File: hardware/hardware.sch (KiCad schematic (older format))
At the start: 54 parts, among them J1 BATT, J2 RFID-RC522, J3 104031-0811, J4 PROG, J5 Conn_01x05_Male, J6 PCM5102A_1, J7 PCM5102A_2, J8 Speakers, SW1 Vol down, SW2 Vol up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

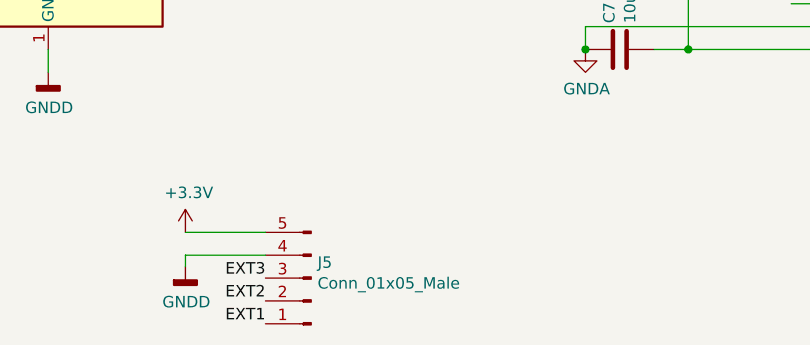
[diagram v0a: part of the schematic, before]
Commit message: fix name of EXT header
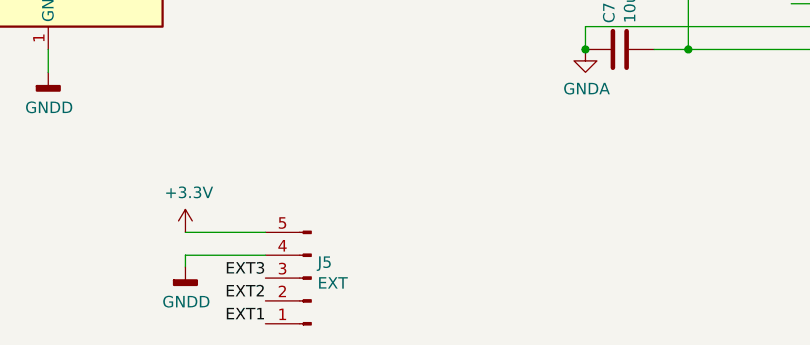
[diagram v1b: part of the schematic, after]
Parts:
- J5: value Conn_01x05_Male -> EXT
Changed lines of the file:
@@
 P 6050 7150
 F 0 "J5" H 6022 7082 50  0000 R CNN
-F 1 "Conn_01x05_Male" H 6022 7173 50  0000 R CNN
+F 1 "EXT" H 6022 7173 50  0000 R CNN
 F 2 "" H 6050 7150 50  0001 C CNN
 F 3 "~" H 6050 7150 50  0001 C CNN

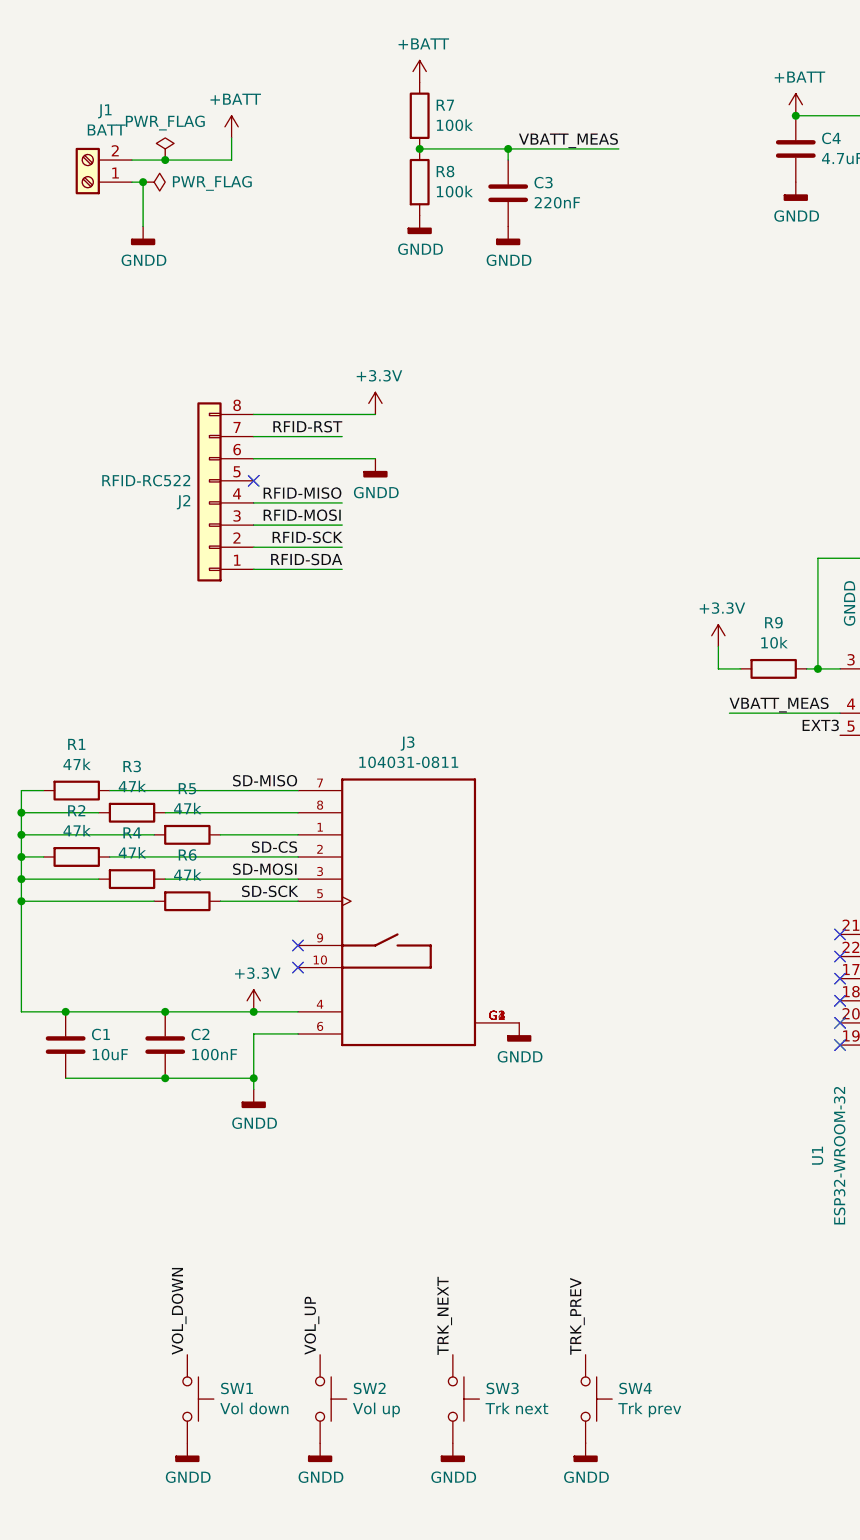
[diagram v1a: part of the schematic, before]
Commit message: layout corrections
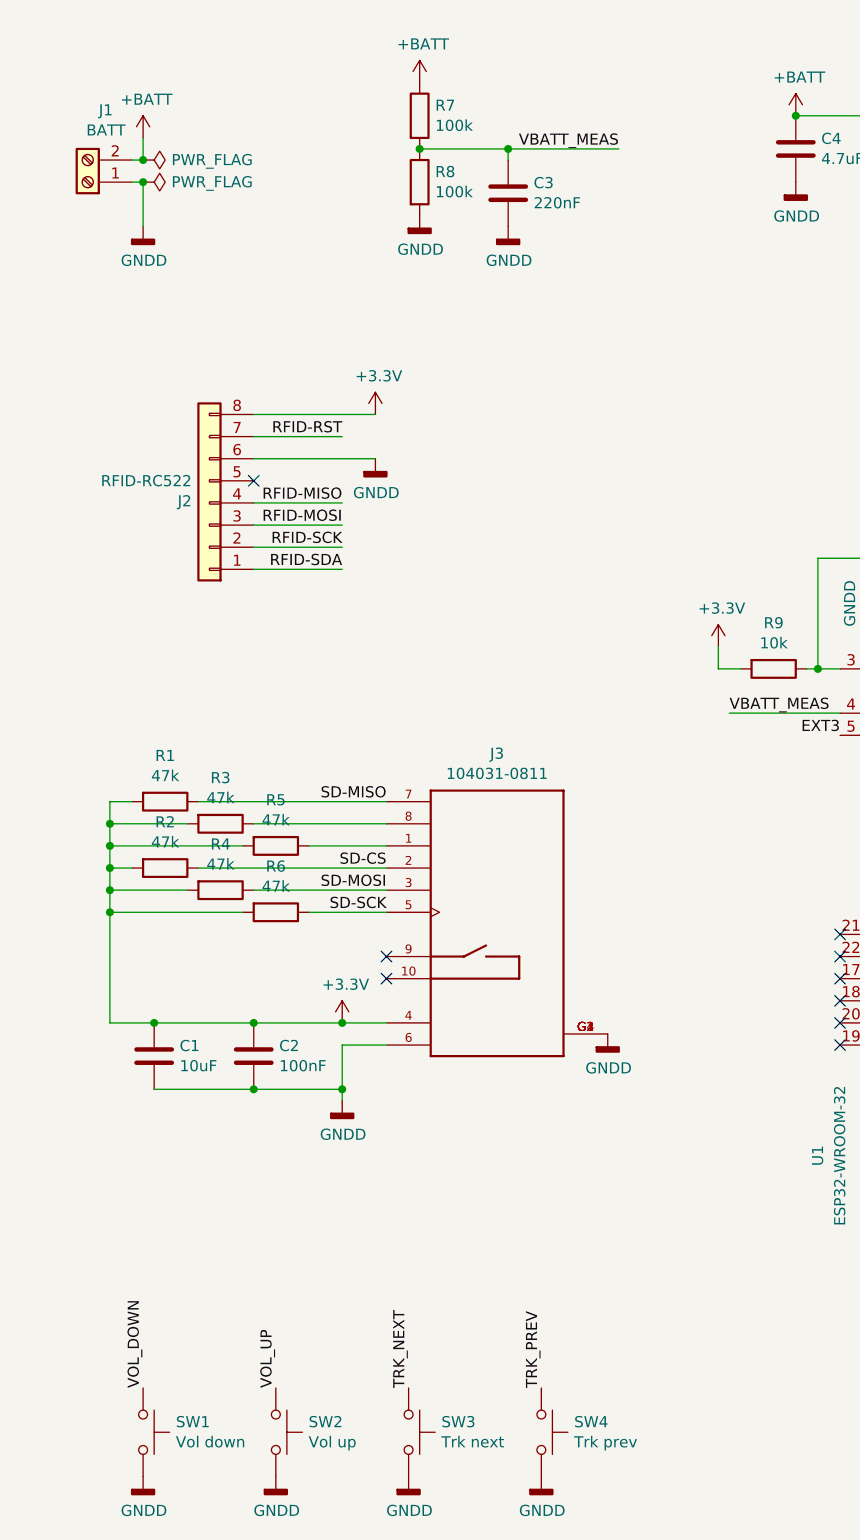
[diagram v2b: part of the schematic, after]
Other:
- moved on the sheet: C1, C2, J3, R1, R2, R3, R4, R5, R6, SW1, SW2, SW3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

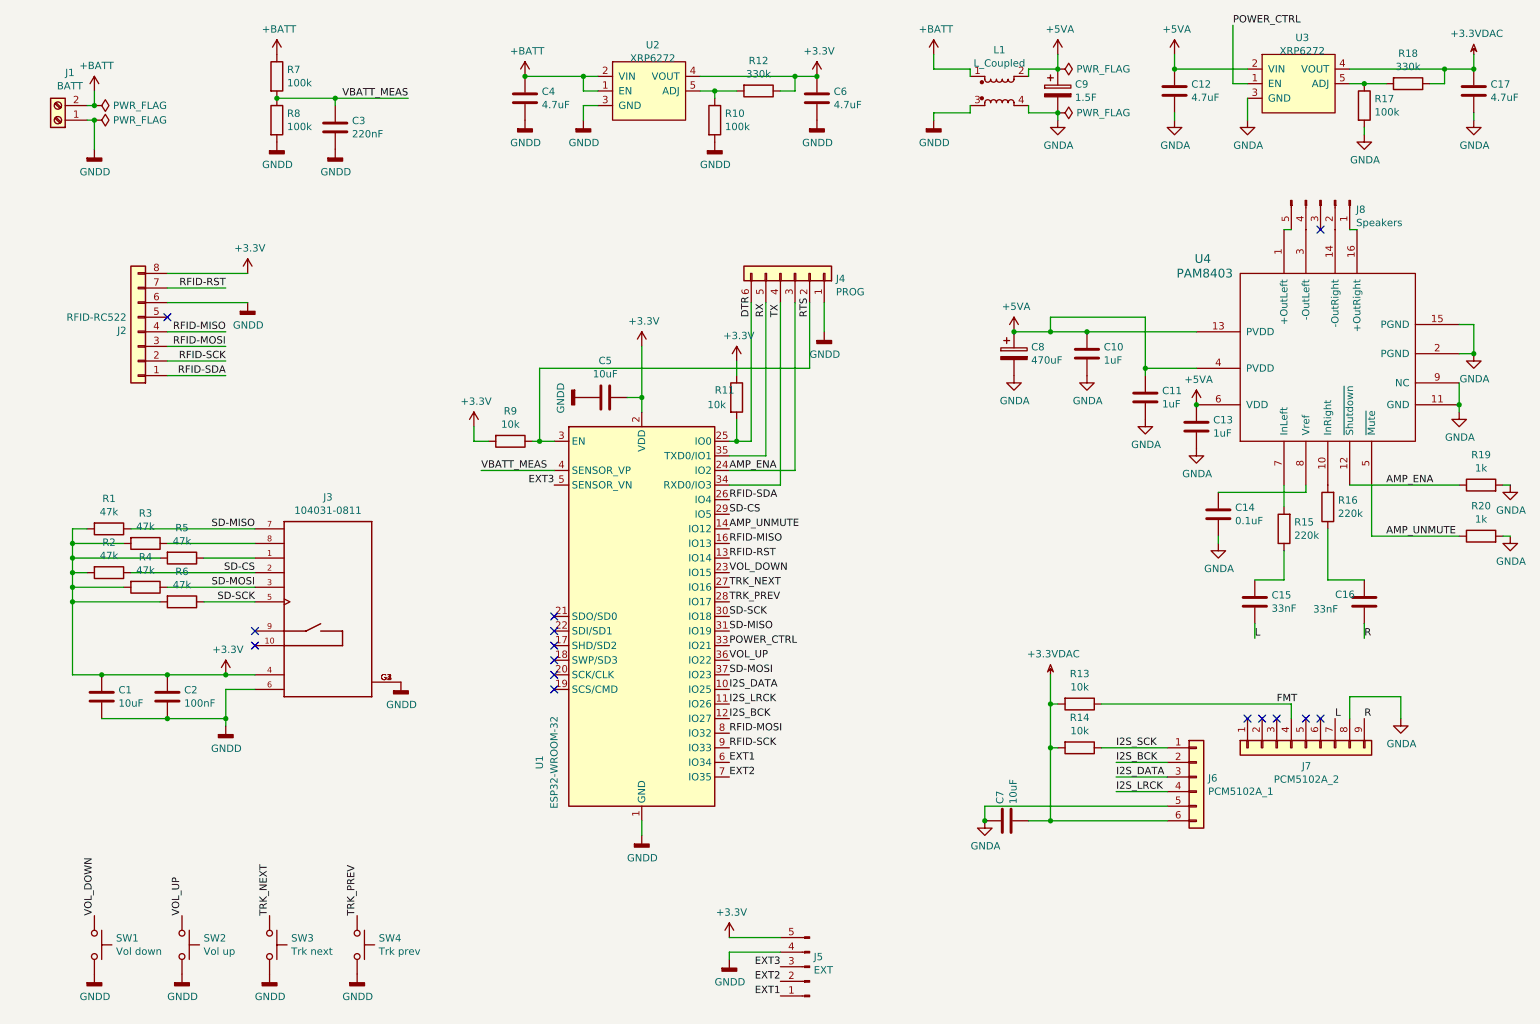
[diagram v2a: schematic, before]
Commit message: use POWER_CTRL to shutdown the amp, AMP_ENA to mute it
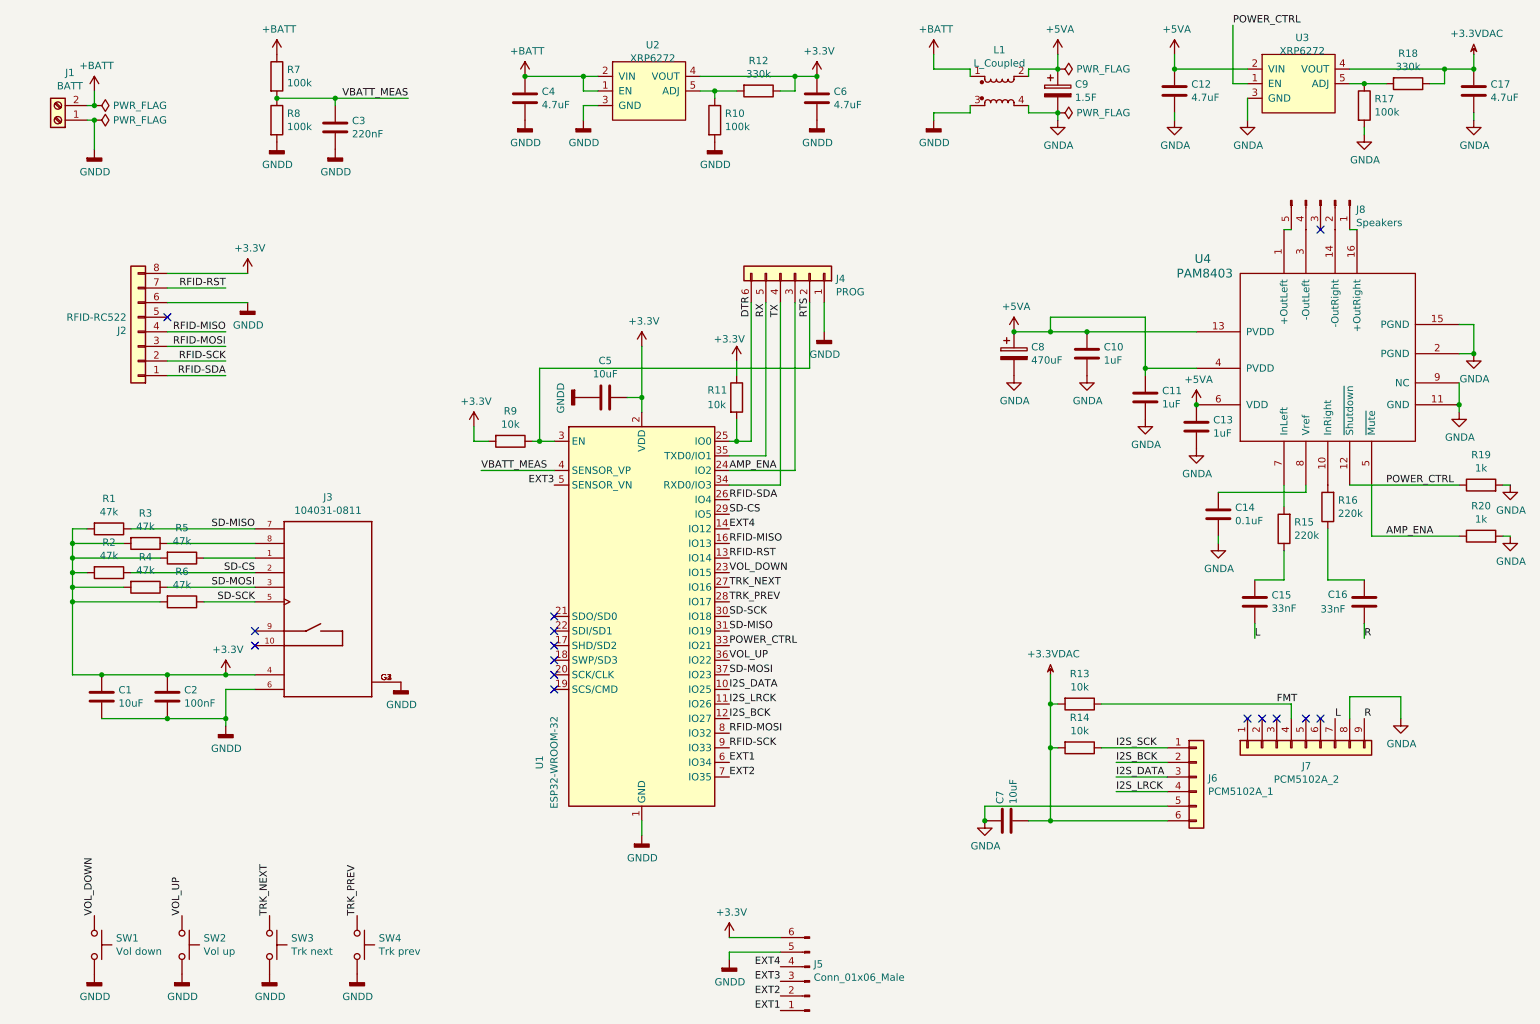
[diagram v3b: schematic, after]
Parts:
- removed J5: EXT, symbol Connector:Conn_01x05_Male
- added J5: Conn_01x06_Male, symbol Connector:Conn_01x06_Male
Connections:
- net +3V3: now also J5.6 (Pin_6)
- net AMP_ENA: now also R20.1, U4.5 (~Mute); no longer R19.1, U4.12 (~Shutdown)
- net EXT1: now also J5.1 (Pin_1)
- net EXT2: now also J5.2 (Pin_2)
- net EXT3: now also J5.3 (Pin_3)
- net GNDD: now also J5.5 (Pin_5)
- net POWER_CTRL: now also R19.1, U4.12 (~Shutdown)
- removed net AMP_UNMUTE: R20.1, U1.14 (IO12), U4.5 (~Mute)
- new net EXT4: J5.4 (Pin_4), U1.14 (IO12)
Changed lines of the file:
@@
 U 1 1 5E73D14D
 P 5550 3250
-F 0 "R11" H 5400 3300 50  0000 L CNN
+F 0 "R11" H 5350 3300 50  0000 L CNN
 F 1 "10k" H 5350 3200 50  0000 L CNN
 F 2 "" V 5480 3250 50  0001 C CNN
@@
 $EndComp
 $Comp
-L power:GNDD #PWR02
+L power:GNDD #PWR03
 U 1 1 5E724B03
 P 1150 7200
-F 0 "#PWR02" H 1150 6950 50  0001 C CNN
+F 0 "#PWR03" H 1150 6950 50  0001 C CNN
 F 1 "GNDD" H 1154 7045 50  0000 C CNN
 F 2 "" H 1150 7200 50  0001 C CNN
@@
 $EndComp
 $Comp
-L power:GNDD #PWR06
+L power:GNDD #PWR04
 U 1 1 5E724CBA
 P 1750 7200
-F 0 "#PWR06" H 1750 6950 50  0001 C CNN
+F 0 "#PWR04" H 1750 6950 50  0001 C CNN
 F 1 "GNDD" H 1754 7045 50  0000 C CNN
 F 2 "" H 1750 7200 50  0001 C CNN
@@
 $EndComp
 $Comp
-L power:GNDD #PWR011
+L power:GNDD #PWR09
 U 1 1 5E724E0D
 P 2350 7200
-F 0 "#PWR011" H 2350 6950 50  0001 C CNN
+F 0 "#PWR09" H 2350 6950 50  0001 C CNN
 F 1 "GNDD" H 2354 7045 50  0000 C CNN
 F 2 "" H 2350 7200 50  0001 C CNN
@@
 $EndComp
 $Comp
-L power:GNDD #PWR014
+L power:GNDD #PWR013
 U 1 1 5E724F18
 P 2950 7200
-F 0 "#PWR014" H 2950 6950 50  0001 C CNN
+F 0 "#PWR013" H 2950 6950 50  0001 C CNN
 F 1 "GNDD" H 2954 7045 50  0000 C CNN
 F 2 "" H 2950 7200 50  0001 C CNN
@@
 	10600 1300 10600 1350
 $Comp
-L Device:C C5
-U 1 1 5E7B8DAB
-P 4650 3250
-F 0 "C5" V 4398 3250 50  0000 C CNN
-F 1 "10uF" V 4489 3250 50  0000 C CNN
-F 2 "" H 4688 3100 50  0001 C CNN
-F 3 "~" H 4650 3250 50  0001 C CNN
-	1    4650 3250
-	0    1    1    0
-$EndComp
-$Comp
 L power:GNDD #PWR019
 U 1 1 5E7BE847
@@
 	4900 3250 4900 3350
 $Comp
-L power:GNDD #PWR01
+L power:GNDD #PWR02
 U 1 1 5E739643
 P 1150 1550
-F 0 "#PWR01" H 1150 1300 50  0001 C CNN
+F 0 "#PWR02" H 1150 1300 50  0001 C CNN
 F 1 "GNDD" H 1154 1395 50  0000 C CNN
 F 2 "" H 1150 1550 50  0001 C CNN
@@
 RFID-SDA
 $Comp
-L power:GNDD #PWR05
+L power:GNDD #PWR06
 U 1 1 5E700E8C
 P 2050 5500
-F 0 "#PWR05" H 2050 5250 50  0001 C CNN
+F 0 "#PWR06" H 2050 5250 50  0001 C CNN
 F 1 "GNDD" H 2054 5345 50  0000 C CNN
 F 2 "" H 2050 5500 50  0001 C CNN
@@
 P 5550 3000
 F 0 "#PWR025" H 5550 2850 50  0001 C CNN
-F 1 "+3.3V" H 5565 3173 50  0000 C CNN
+F 1 "+3.3V" H 5500 3150 50  0000 C CNN
 F 2 "" H 5550 3000 50  0001 C CNN
 F 3 "" H 5550 3000 50  0001 C CNN
@@
 	1150 1350 1150 1550
 $Comp
-L power:+BATT #PWR03
+L power:+BATT #PWR01
 U 1 1 5EC2E9DA
 P 1150 1150
-F 0 "#PWR03" H 1150 1000 50  0001 C CNN
+F 0 "#PWR01" H 1150 1000 50  0001 C CNN
 F 1 "+BATT" H 1165 1323 50  0000 C CNN
 F 2 "" H 1150 1150 50  0001 C CNN
@@
 $EndComp
 $Comp
-L power:+BATT #PWR09
+L power:+BATT #PWR010
 U 1 1 5EC4670E
 P 2400 900
-F 0 "#PWR09" H 2400 750 50  0001 C CNN
+F 0 "#PWR010" H 2400 750 50  0001 C CNN
 F 1 "+BATT" H 2415 1073 50  0000 C CNN
 F 2 "" H 2400 900 50  0001 C CNN
@@
 $EndComp
 $Comp
-L power:GNDD #PWR010
+L power:GNDD #PWR011
 U 1 1 5EC4692A
 P 2400 1500
-F 0 "#PWR010" H 2400 1250 50  0001 C CNN
+F 0 "#PWR011" H 2400 1250 50  0001 C CNN
 F 1 "GNDD" H 2404 1345 50  0000 C CNN
 F 2 "" H 2400 1500 50  0001 C CNN
@@
 $EndComp
 $Comp
-L power:+3.3V #PWR04
+L power:+3.3V #PWR05
 U 1 1 5ECC2179
 P 2050 5150
-F 0 "#PWR04" H 2050 5000 50  0001 C CNN
+F 0 "#PWR05" H 2050 5000 50  0001 C CNN
 F 1 "+3.3V" H 2065 5323 50  0000 C CNN
 F 2 "" H 2050 5150 50  0001 C CNN
@@
 U 1 1 5EFB2FFE
 P 9850 4650
-F 0 "C16" H 10050 4600 50  0000 R CNN
-F 1 "33nF" H 10200 4700 50  0000 R CNN
+F 0 "C16" H 10100 4600 50  0000 R CNN
+F 1 "33nF" H 10150 4700 50  0000 R CNN
 F 2 "" H 9888 4500 50  0001 C CNN
 F 3 "~" H 9850 4650 50  0001 C CNN
@@
 	0    -1   -1   0
 $EndComp
-Text Label 10000 3850 0    50   ~ 0
+Text Label 10000 4200 0    50   ~ 0
 AMP_ENA
 $Comp
@@
 NoConn ~ 4300 5150
 NoConn ~ 4300 5250
-Text Label 5500 4150 0    50   ~ 0
-AMP_UNMUTE
 Text Label 5500 5750 0    50   ~ 0
 EXT1
@@
 Text Label 4300 3850 2    50   ~ 0
 EXT3
+Text Label 5850 7450 2    50   ~ 0
+EXT1
 Text Label 5850 7350 2    50   ~ 0
-EXT1
+EXT2
 Text Label 5850 7250 2    50   ~ 0
-EXT2
-Text Label 5850 7150 2    50   ~ 0
 EXT3
 $Comp
@@
 	8850 4200 8850 4250
 $Comp
-L power:PWR_FLAG #FLG02
+L power:PWR_FLAG #FLG01
 U 1 1 5ED6A703
 P 1150 1250
-F 0 "#FLG02" H 1150 1325 50  0001 C CNN
+F 0 "#FLG01" H 1150 1325 50  0001 C CNN
 F 1 "PWR_FLAG" V 1150 1378 50  0000 L CNN
 F 2 "" H 1150 1250 50  0001 C CNN
@@
 $EndComp
 $Comp
-L power:GNDD #PWR013
+L power:GNDD #PWR014
 U 1 1 5ED6B633
 P 3250 5200
-F 0 "#PWR013" H 3250 4950 50  0001 C CNN
+F 0 "#PWR014" H 3250 4950 50  0001 C CNN
 F 1 "GNDD" H 3254 5045 50  0000 C CNN
 F 2 "" H 3250 5200 50  0001 C CNN
@@
 $EndComp
 $Comp
-L power:PWR_FLAG #FLG01
+L power:PWR_FLAG #FLG02
 U 1 1 5ED6BC4B
 P 1150 1350
-F 0 "#FLG01" H 1150 1425 50  0001 C CNN
+F 0 "#FLG02" H 1150 1425 50  0001 C CNN
 F 1 "PWR_FLAG" V 1150 1478 50  0000 L CNN
 F 2 "" H 1150 1350 50  0001 C CNN
@@
 Wire Wire Line
 	9900 3850 9900 4200
-Text Label 10000 4200 0    50   ~ 0
-AMP_UNMUTE
 Wire Wire Line
 	9750 3850 10500 3850
-$Comp
-L Connector:Conn_01x05_Male J5
-U 1 1 5ED9429D
-P 6050 7150
-F 0 "J5" H 6022 7082 50  0000 R CNN
-F 1 "EXT" H 6022 7173 50  0000 R CNN
-F 2 "" H 6050 7150 50  0001 C CNN
-F 3 "~" H 6050 7150 50  0001 C CNN
-	1    6050 7150
-	-1   0    0    1
-$EndComp
 Wire Wire Line
 	1100 1250 1150 1250
@@
 	1150 1150 1150 1250
 Connection ~ 1150 1250
+$Comp
+L Device:C C5
+U 1 1 5E7B8DAB
+P 4650 3250
+F 0 "C5" V 4398 3250 50  0000 C CNN
+F 1 "10uF" V 4489 3250 50  0000 C CNN
+F 2 "" H 4688 3100 50  0001 C CNN
+F 3 "~" H 4650 3250 50  0001 C CNN
+	1    4650 3250
+	0    1    1    0
+$EndComp
+Text Label 10000 3850 0    50   ~ 0
+POWER_CTRL
+$Comp
+L Connector:Conn_01x06_Male J5
+U 1 1 5EDAF37C
+P 6050 7250
+F 0 "J5" H 6022 7132 50  0000 R CNN
+F 1 "Conn_01x06_Male" H 6022 7223 50  0000 R CNN
+F 2 "" H 6050 7250 50  0001 C CNN
+F 3 "~" H 6050 7250 50  0001 C CNN
+	1    6050 7250
+	-1   0    0    1
+$EndComp
+Text Label 5850 7150 2    50   ~ 0
+EXT4
+Text Label 5500 4150 0    50   ~ 0
+EXT4
 $EndSCHEMATC

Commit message: add reset button
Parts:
- added SW?: Reset, symbol Switch:SW_Push
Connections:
- net GNDD: now also SW?.2
- net RTS renamed RESET
- net RESET: now also SW?.1
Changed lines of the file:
@@
 EESchema Schematic File Version 4
+LIBS:hardware-cache
 EELAYER 30 0
 EELAYER END
@@
 Text Label 5500 4150 0    50   ~ 0
 EXT4
+$Comp
+L Switch:SW_Push SW?
+U 1 1 5ECDD608
+P 3600 7000
+F 0 "SW?" V 3554 7148 50  0000 L CNN
+F 1 "Reset" V 3645 7148 50  0000 L CNN
+F 2 "" H 3600 7200 50  0001 C CNN
+F 3 "~" H 3600 7200 50  0001 C CNN
+	1    3600 7000
+	0    1    1    0
+$EndComp
+$Comp
+L power:GNDD #PWR?
+U 1 1 5ECDDABA
+P 3600 7200
+F 0 "#PWR?" H 3600 6950 50  0001 C CNN
+F 1 "GNDD" H 3604 7045 50  0000 C CNN
+F 2 "" H 3600 7200 50  0001 C CNN
+F 3 "" H 3600 7200 50  0001 C CNN
+	1    3600 7200
+	1    0    0    -1
+$EndComp
+Text Label 3600 6800 1    50   ~ 0
+RESET
+Text Label 4200 3300 1    50   ~ 0
+RESET
 $EndSCHEMATC

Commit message: fixed annotation
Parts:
- gave numbers to parts that had none: 1
